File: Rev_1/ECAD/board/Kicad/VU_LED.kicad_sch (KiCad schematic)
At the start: 11 parts, among them Q1 PMOS, Q2 NMOS

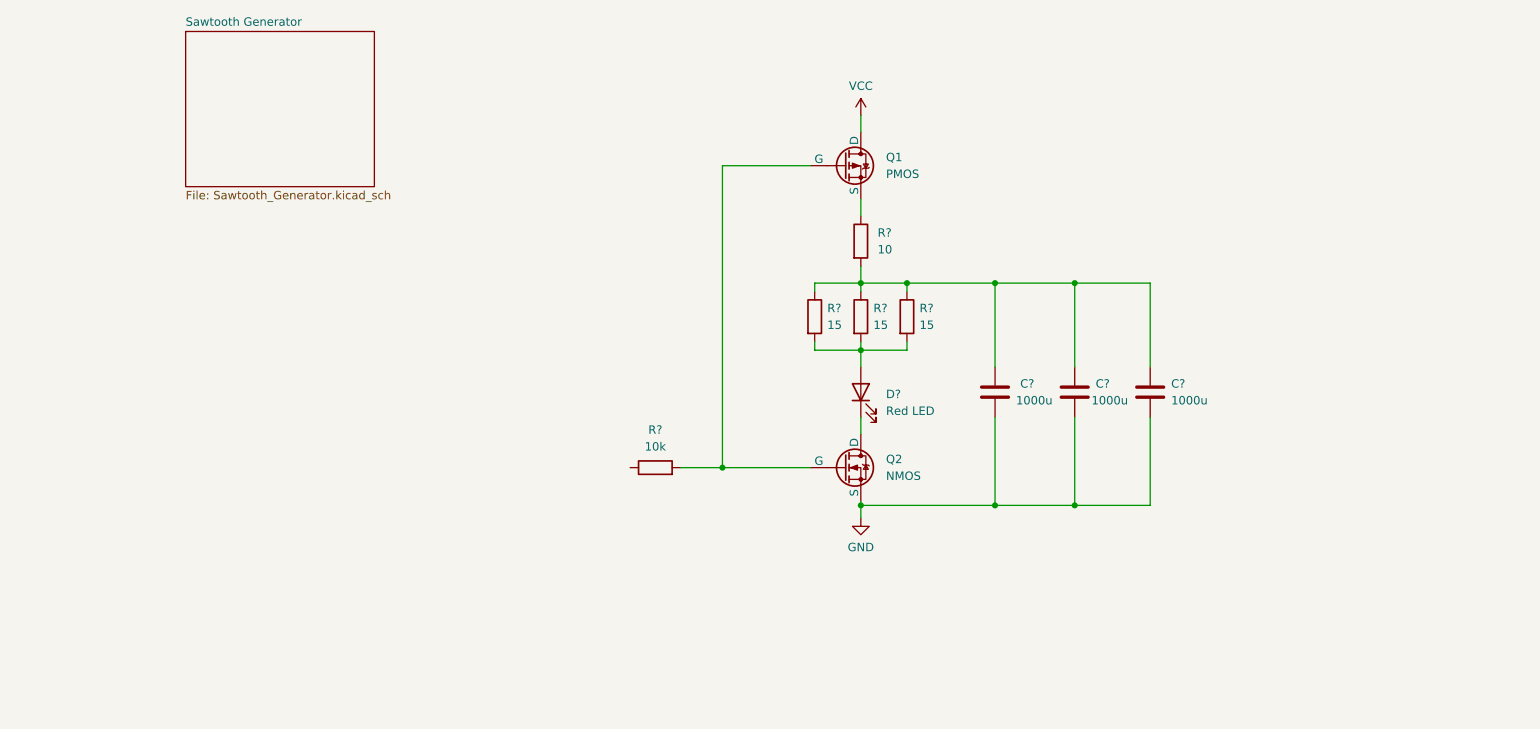
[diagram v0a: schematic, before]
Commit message: Added filter hierarchy
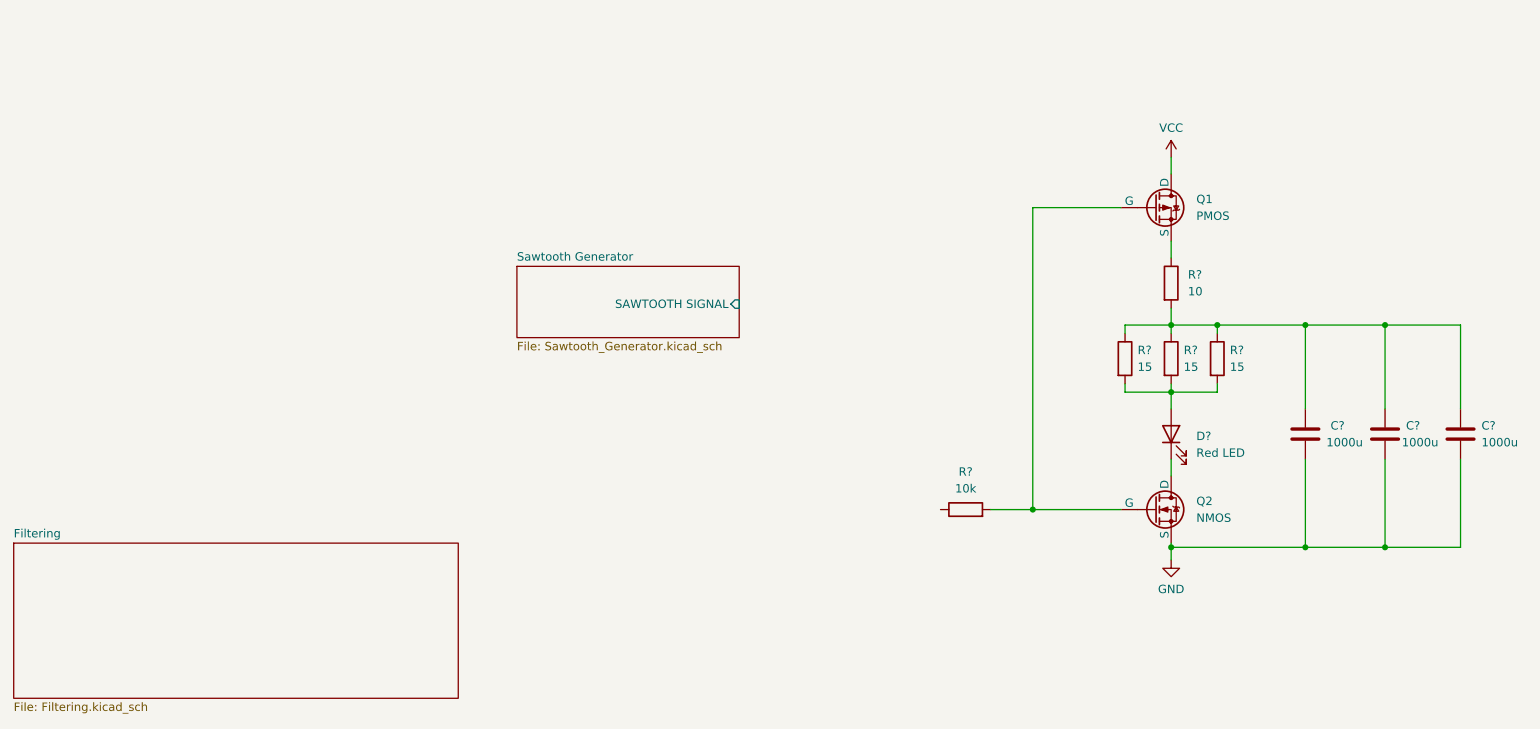
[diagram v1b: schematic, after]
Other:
- added sheet Filtering (Filtering.kicad_sch)
- sheet Sawtooth Generator ports: added SAWTOOTH SIGNAL; removed none
- moved on the sheet: C?, D?, Q1, Q2, R?

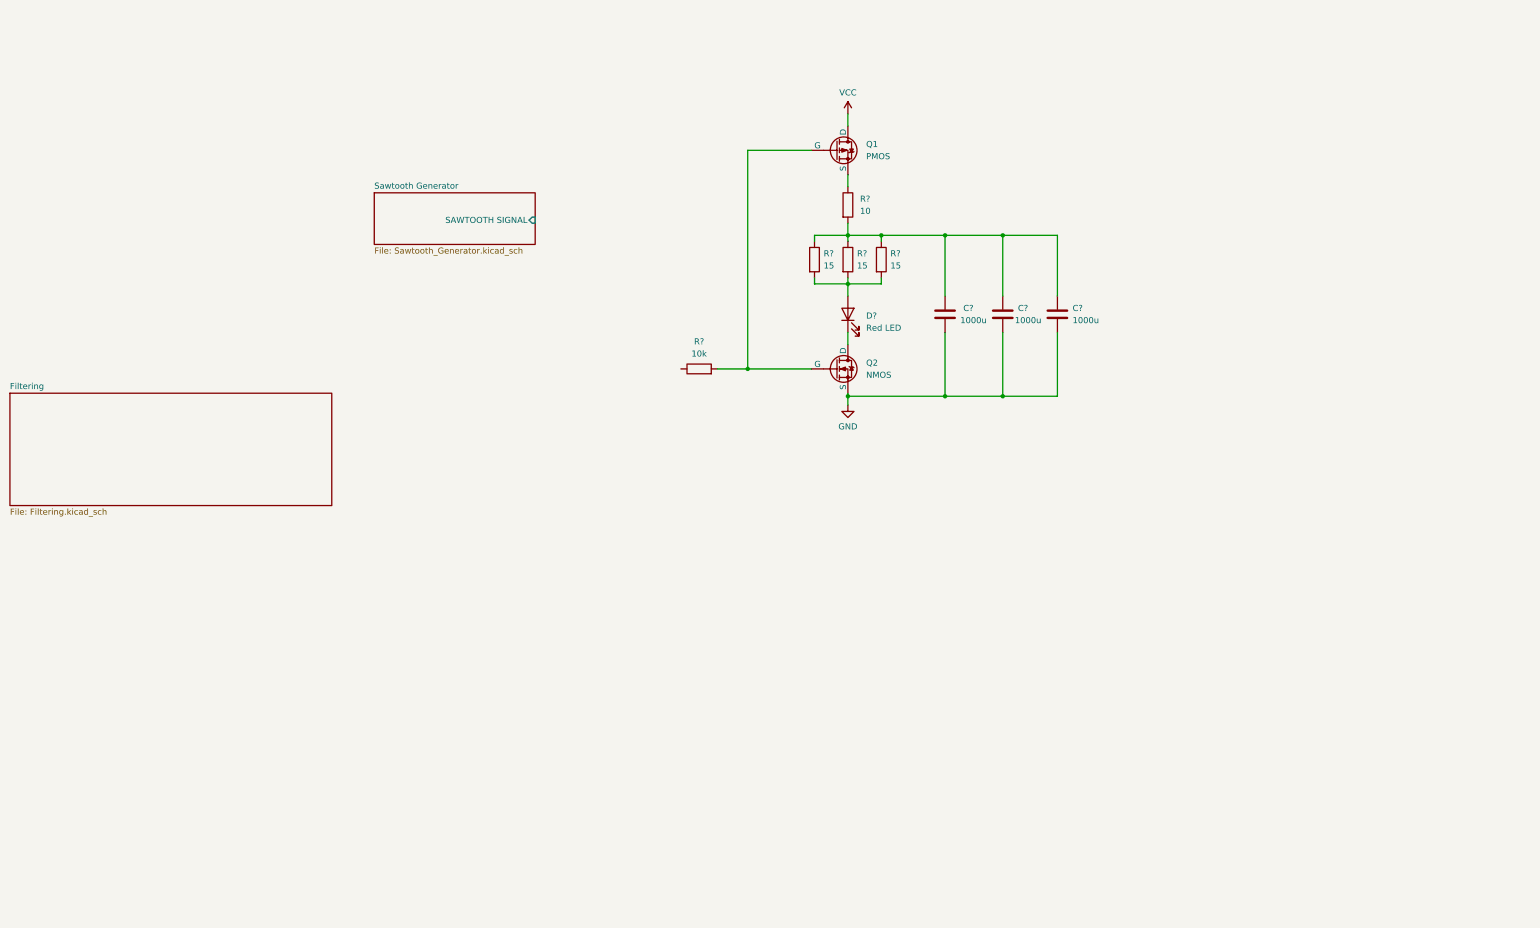
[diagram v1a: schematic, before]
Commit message: Added gain and rectifier stage
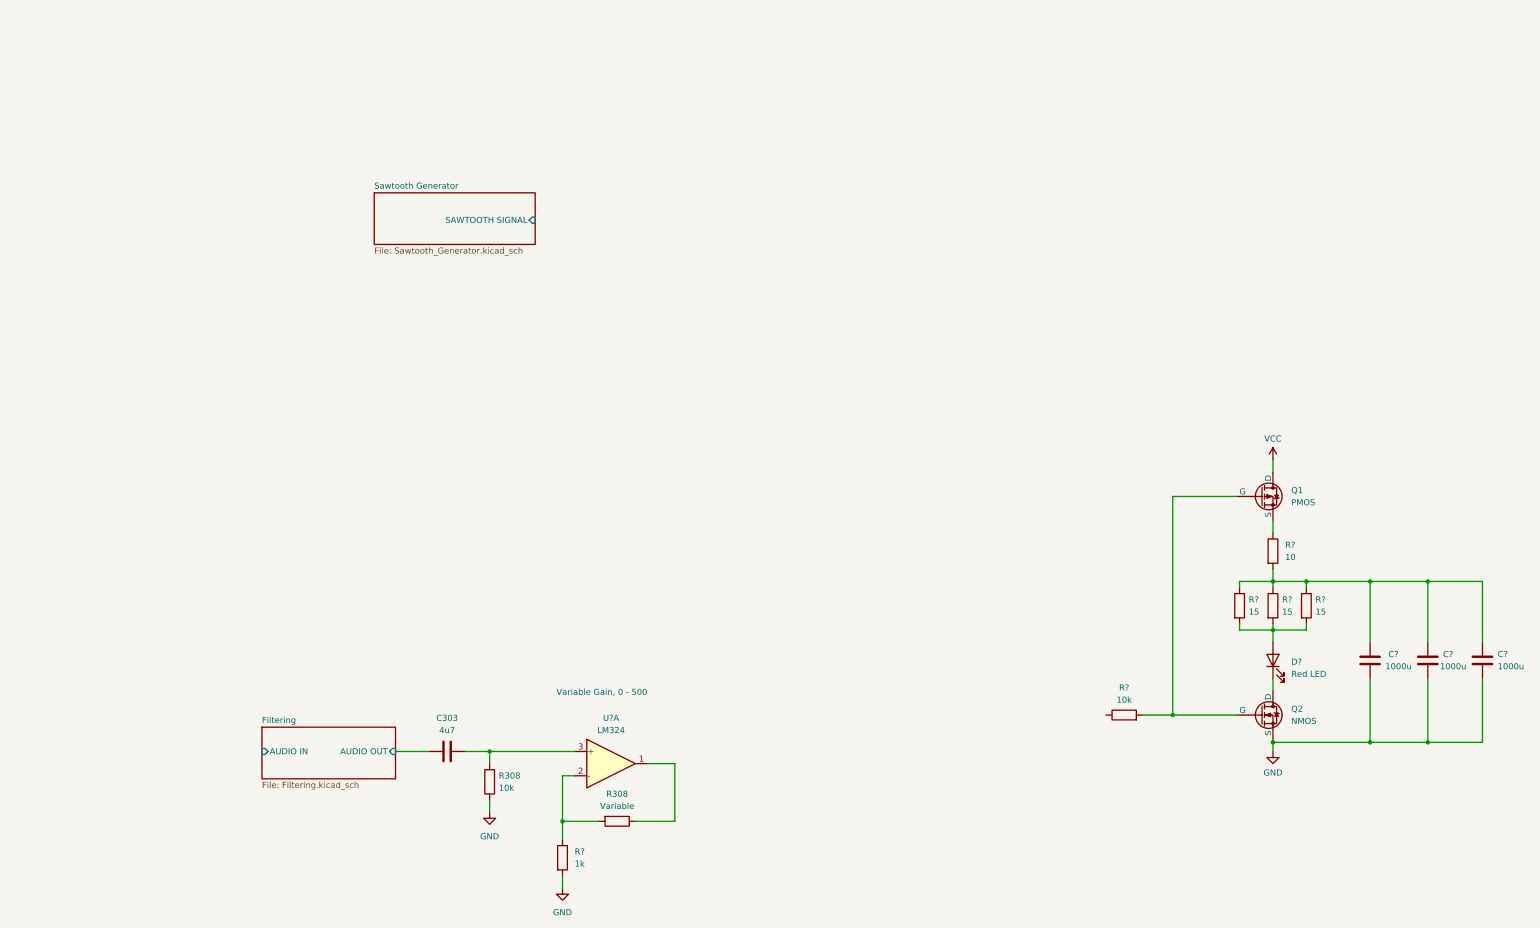
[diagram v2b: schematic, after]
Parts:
- added C303: 4u7, Capacitor_SMD:C_0805_2012Metric_Pad1.18x1.45mm_HandSolder, symbol Device:C
- added R308: 10k, Resistor_SMD:R_0805_2012Metric_Pad1.20x1.40mm_HandSolder, symbol Device:R
- added R308: Variable, Resistor_SMD:R_0805_2012Metric_Pad1.20x1.40mm_HandSolder, symbol Device:R
- added R?: 1k, symbol Device:R
- added U?: LM324, symbol Amplifier_Operational:LM324
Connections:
- net GND: now also R308.1, R?.2
- new net: R308.2, R?.1, U?.2 (-)
- new net: R308.1, U?.1
- new net: C303.2, R308.2, U?.3 (+)
- new net Filtering/AUDIO OUT: C303.1
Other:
- sheet Filtering ports: added AUDIO IN, AUDIO OUT; removed none
- note added: "Variable Gain, 0 - 500"
- moved on the sheet: C?, D?, Q1, Q2, R?

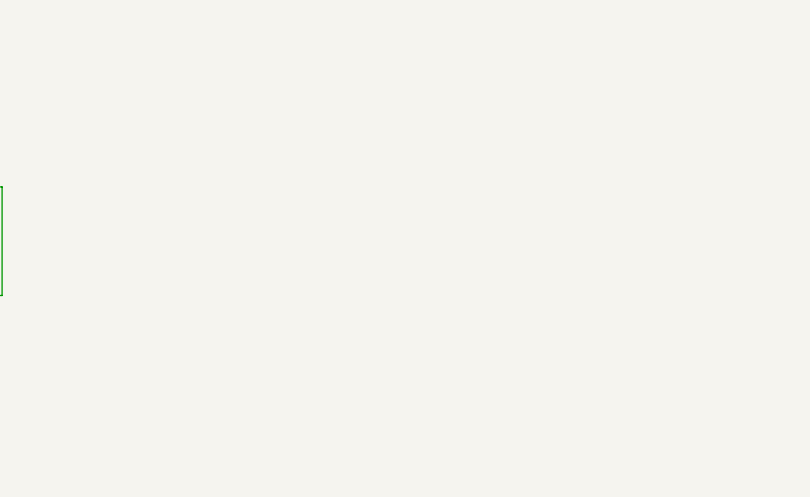
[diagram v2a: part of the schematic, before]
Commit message: Added gain and rectifier stage
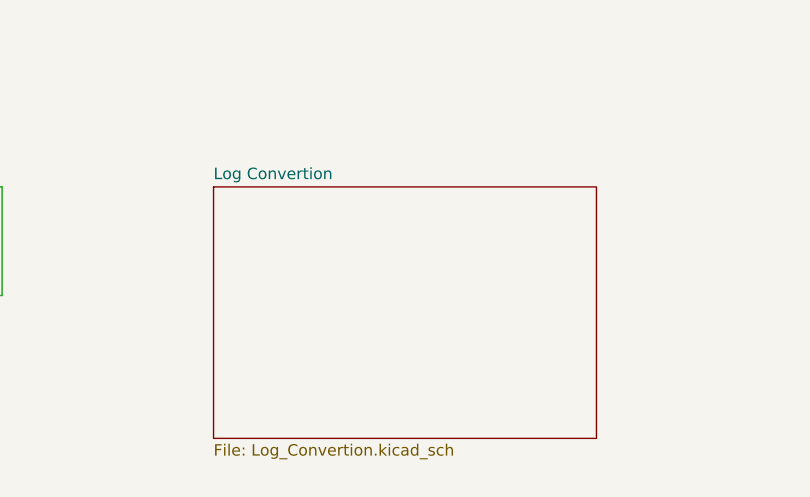
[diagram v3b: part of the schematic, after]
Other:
- added sheet Log Convertion (Log_Convertion.kicad_sch)
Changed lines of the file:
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@@
+    )
+  )
+  (sheet (at 205.74 203.835) (size 42.545 27.94) (fields_autoplaced)
+    (stroke (width 0.1524) (type solid))
+    (fill (color 0 0 0 0.0000))
+    (property "Sheetname" "Log Convertion" (at 205.74 203.1234 0)
+      (effects (font (size 1.27 1.27)) (justify left bottom))
+    )
+    (property "Sheetfile" "Log_Convertion.kicad_sch" (at 205.74 232.3596 0)
+      (effects (font (size 1.27 1.27)) (justify left top))
+    )
+    (instances
+      (project "VU_LED"
+        (path "/7cb59420-42b3-42c5-b41a-eedd7f57e790" (page "4"))
+      )
     )
   )
